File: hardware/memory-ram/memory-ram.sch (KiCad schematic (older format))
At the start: 27 parts, among them J1 Conn_Mem_Ext, J2 Conn_Power, U1 IS61WV5128EDBLL-10TLI, U2 74LVC1G86, U3 MIC5504-3.3YM5, U4 74LVC1G32, U5 74LVC1G332, U6 74LVC1G86, U7 74LVC1G04

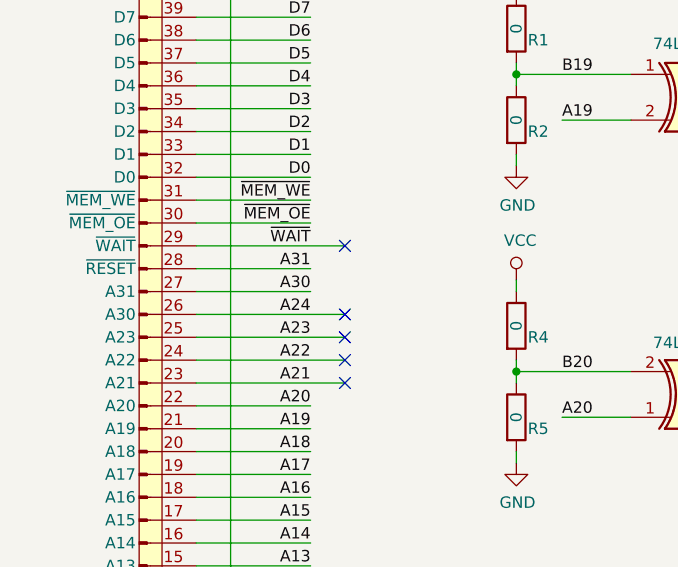
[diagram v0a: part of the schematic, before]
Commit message: Added ~RESET to memory bus
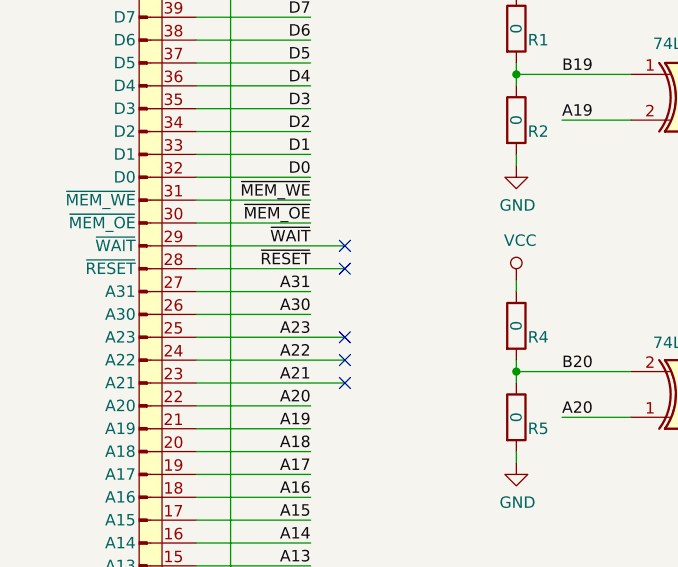
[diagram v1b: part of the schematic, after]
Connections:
- net A24 is gone; now on net A30: J1.26 (A30)
- net A30: no longer J1.27 (A31)
- net A31: now also J1.27 (A31); no longer J1.28 (~RESET)
- new net ~RESET: J1.28 (~RESET)
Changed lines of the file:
@@
 Text Label 1750 3600 2    50   ~ 0
 A23
-Text Label 1750 3500 2    50   ~ 0
-A24
 Text Label 1750 3200 2    50   ~ 0
 ~WAIT
@@
 Wire Wire Line
 	1750 4200 1250 4200
-Text Label 1750 3300 2    50   ~ 0
+Text Label 1750 3400 2    50   ~ 0
 A31
-Text Label 1750 3400 2    50   ~ 0
+Text Label 1750 3500 2    50   ~ 0
 A30
 Wire Wire Line
-	1750 3300 1250 3300
-Wire Wire Line
-	1250 3400 1750 3400
+	1750 3400 1250 3400
+Wire Wire Line
+	1250 3500 1750 3500
 $Comp
 L riscv-serial:Conn_Power J?
@@
 Wire Wire Line
 	1250 3600 1900 3600
-Wire Wire Line
-	1250 3500 1900 3500
-NoConn ~ 1900 3500
 NoConn ~ 1900 3600
 NoConn ~ 1900 3700
@@
 	5600 6550 4850 6550
 Connection ~ 4850 6550
+Wire Wire Line
+	1250 3300 1900 3300
+NoConn ~ 1900 3300
+Text Label 1750 3300 2    50   ~ 0
+~RESET
 $EndSCHEMATC

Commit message: Unified footprints
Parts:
- D1: footprint LED_SMD:LED_0805_2012Metric -> LED_SMD:LED_0805_2012Metric_Pad1.15x1.40mm_HandSolder
- R1, R2, R3, R4, R5: footprint Resistor_SMD:R_0805_2012Metric -> Resistor_SMD:R_0805_2012Metric_Pad1.15x1.40mm_HandSolder
- U2, U3, U4, U6, U7: footprint Package_TO_SOT_SMD:SOT-23-5 -> Package_TO_SOT_SMD:SOT-23-5_HandSoldering
- U5: footprint Package_TO_SOT_SMD:SOT-23-6 -> Package_TO_SOT_SMD:SOT-23-6_Handsoldering
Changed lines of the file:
@@
 F 0 "U3" H 7900 6117 50  0000 C CNN
 F 1 "MIC5504-3.3YM5" H 7900 6026 50  0000 C CNN
-F 2 "Package_TO_SOT_SMD:SOT-23-5" H 7900 5350 50  0001 C CNN
+F 2 "Package_TO_SOT_SMD:SOT-23-5_HandSoldering" H 7900 5350 50  0001 C CNN
 F 3 "http://ww1.microchip.com/downloads/en/DeviceDoc/MIC550X.pdf" H 7650 6000 50  0001 C CNN
 	1    7900 5750
@@
 F 0 "U5" H 5500 3033 50  0000 C CNN
 F 1 "74LVC1G332" H 5500 3124 50  0000 C CNN
-F 2 "Package_TO_SOT_SMD:SOT-23-6" H 5470 3320 50  0001 C CNN
+F 2 "Package_TO_SOT_SMD:SOT-23-6_Handsoldering" H 5470 3320 50  0001 C CNN
 F 3 "" H 5470 3320 50  0001 C CNN
 	1    5500 3350
@@
 F 0 "R1" H 2700 2200 50  0000 L CNN
 F 1 "0" V 2650 2250 50  0000 C CNN
-F 2 "Resistor_SMD:R_0805_2012Metric" V 2580 2250 50  0001 C CNN
+F 2 "Resistor_SMD:R_0805_2012Metric_Pad1.15x1.40mm_HandSolder" V 2580 2250 50  0001 C CNN
 F 3 "~" H 2650 2250 50  0001 C CNN
 	1    2650 2250
@@
 F 0 "R2" H 2700 2600 50  0000 L CNN
 F 1 "0" V 2650 2650 50  0000 C CNN
-F 2 "Resistor_SMD:R_0805_2012Metric" V 2580 2650 50  0001 C CNN
+F 2 "Resistor_SMD:R_0805_2012Metric_Pad1.15x1.40mm_HandSolder" V 2580 2650 50  0001 C CNN
 F 3 "~" H 2650 2650 50  0001 C CNN
 	1    2650 2650
@@
 F 0 "R4" H 2700 3500 50  0000 L CNN
 F 1 "0" V 2650 3550 50  0000 C CNN
-F 2 "Resistor_SMD:R_0805_2012Metric" V 2580 3550 50  0001 C CNN
+F 2 "Resistor_SMD:R_0805_2012Metric_Pad1.15x1.40mm_HandSolder" V 2580 3550 50  0001 C CNN
 F 3 "~" H 2650 3550 50  0001 C CNN
 	1    2650 3550
@@
 F 0 "R5" H 2700 3900 50  0000 L CNN
 F 1 "0" V 2650 3950 50  0000 C CNN
-F 2 "Resistor_SMD:R_0805_2012Metric" V 2580 3950 50  0001 C CNN
+F 2 "Resistor_SMD:R_0805_2012Metric_Pad1.15x1.40mm_HandSolder" V 2580 3950 50  0001 C CNN
 F 3 "~" H 2650 3950 50  0001 C CNN
 	1    2650 3950
@@
 F 0 "U4" H 4400 3600 50  0000 C CNN
 F 1 "74LVC1G32" H 4400 3484 50  0000 C CNN
-F 2 "Package_TO_SOT_SMD:SOT-23-5" H 4370 3220 50  0001 C CNN
+F 2 "Package_TO_SOT_SMD:SOT-23-5_HandSoldering" H 4370 3220 50  0001 C CNN
 F 3 "" H 4370 3220 50  0001 C CNN
 	1    4400 3250
@@
 F 0 "U6" H 3450 3533 50  0000 C CNN
 F 1 "74LVC1G86" H 3450 3624 50  0000 C CNN
-F 2 "Package_TO_SOT_SMD:SOT-23-5" H 3420 3820 50  0001 C CNN
+F 2 "Package_TO_SOT_SMD:SOT-23-5_HandSoldering" H 3420 3820 50  0001 C CNN
 F 3 "" H 3420 3820 50  0001 C CNN
 	1    3450 3850
@@
 F 0 "U2" H 3450 2875 50  0000 C CNN
 F 1 "74LVC1G86" H 3450 2784 50  0000 C CNN
-F 2 "Package_TO_SOT_SMD:SOT-23-5" H 3420 2520 50  0001 C CNN
+F 2 "Package_TO_SOT_SMD:SOT-23-5_HandSoldering" H 3420 2520 50  0001 C CNN
 F 3 "" H 3420 2520 50  0001 C CNN
 	1    3450 2550
@@
 F 0 "U2" H 3530 5996 50  0000 L CNN
 F 1 "74LVC1G86" H 3530 5905 50  0000 L CNN
-F 2 "Package_TO_SOT_SMD:SOT-23-5" H 3370 5920 50  0001 C CNN
+F 2 "Package_TO_SOT_SMD:SOT-23-5_HandSoldering" H 3370 5920 50  0001 C CNN
 F 3 "" H 3370 5920 50  0001 C CNN
 	2    3400 5950
@@
 F 0 "U6" H 4280 5996 50  0000 L CNN
 F 1 "74LVC1G86" H 4280 5905 50  0000 L CNN
-F 2 "Package_TO_SOT_SMD:SOT-23-5" H 4120 5920 50  0001 C CNN
+F 2 "Package_TO_SOT_SMD:SOT-23-5_HandSoldering" H 4120 5920 50  0001 C CNN
 F 3 "" H 4120 5920 50  0001 C CNN
 	2    4150 5950
@@
 F 0 "U4" H 5050 6050 50  0000 C CNN
 F 1 "74LVC1G32" H 5200 5950 50  0000 C CNN
-F 2 "Package_TO_SOT_SMD:SOT-23-5" H 4820 5920 50  0001 C CNN
+F 2 "Package_TO_SOT_SMD:SOT-23-5_HandSoldering" H 4820 5920 50  0001 C CNN
 F 3 "" H 4820 5920 50  0001 C CNN
 	2    4850 5950
@@
 F 0 "U5" H 2780 5996 50  0000 L CNN
 F 1 "74LVC1G332" H 2780 5905 50  0000 L CNN
-F 2 "Package_TO_SOT_SMD:SOT-23-6" H 2620 5920 50  0001 C CNN
+F 2 "Package_TO_SOT_SMD:SOT-23-6_Handsoldering" H 2620 5920 50  0001 C CNN
 F 3 "" H 2620 5920 50  0001 C CNN
 	2    2650 5950
@@
 F 0 "R3" H 10150 2950 50  0000 L CNN
 F 1 "330" V 10100 3000 50  0000 C CNN
-F 2 "Resistor_SMD:R_0805_2012Metric" V 10030 3000 50  0001 C CNN
+F 2 "Resistor_SMD:R_0805_2012Metric_Pad1.15x1.40mm_HandSolder" V 10030 3000 50  0001 C CNN
 F 3 "~" H 10100 3000 50  0001 C CNN
 	1    10100 3000
@@
 F 0 "D1" V 10138 2383 50  0000 R CNN
 F 1 "LED" V 10047 2383 50  0000 R CNN
-F 2 "LED_SMD:LED_0805_2012Metric" H 10100 2500 50  0001 C CNN
+F 2 "LED_SMD:LED_0805_2012Metric_Pad1.15x1.40mm_HandSolder" H 10100 2500 50  0001 C CNN
 F 3 "~" H 10100 2500 50  0001 C CNN
 	1    10100 2500
@@
 F 0 "U7" H 4400 3550 50  0000 C CNN
 F 1 "74LVC1G04" H 4400 3650 50  0000 C CNN
-F 2 "Package_TO_SOT_SMD:SOT-23-5" H 4400 3850 50  0001 C CNN
+F 2 "Package_TO_SOT_SMD:SOT-23-5_HandSoldering" H 4400 3850 50  0001 C CNN
 F 3 "" H 4400 3850 50  0001 C CNN
 	1    4400 3850
@@
 F 0 "U7" H 5800 6000 50  0000 C CNN
 F 1 "74LVC1G04" H 5950 5900 50  0000 C CNN
-F 2 "Package_TO_SOT_SMD:SOT-23-5" H 5600 5950 50  0001 C CNN
+F 2 "Package_TO_SOT_SMD:SOT-23-5_HandSoldering" H 5600 5950 50  0001 C CNN
 F 3 "" H 5600 5950 50  0001 C CNN
 	2    5600 5950

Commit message: Added test points
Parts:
- added TP1: TestPoint, TestPoint:TestPoint_THTPad_D2.0mm_Drill1.0mm, symbol Connector:TestPoint
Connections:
- net GND: now also TP1.1
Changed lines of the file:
@@
 	8150 1800 8400 1800
 $Comp
-L power:VCC #PWR01
+L power:VCC #PWR?
 U 1 1 5ED06DC6
 P 7550 1550
-F 0 "#PWR01" H 7550 1400 50  0001 C CNN
+F 0 "#PWR?" H 7550 1400 50  0001 C CNN
 F 1 "VCC" H 7567 1723 50  0000 C CNN
 F 2 "" H 7550 1550 50  0001 C CNN
@@
 	7550 1550 7550 1600
 $Comp
-L power:GND #PWR03
+L power:GND #PWR?
 U 1 1 5ED072CF
 P 7550 4250
-F 0 "#PWR03" H 7550 4000 50  0001 C CNN
+F 0 "#PWR?" H 7550 4000 50  0001 C CNN
 F 1 "GND" H 7555 4077 50  0000 C CNN
 F 2 "" H 7550 4250 50  0001 C CNN
@@
 P 1400 6100
 AR Path="/5ED0998A/5ED5DB0E" Ref="#PWR?"  Part="1"
-AR Path="/5ED5DB0E" Ref="#PWR05"  Part="1"
-F 0 "#PWR05" H 1400 5850 50  0001 C CNN
+AR Path="/5ED5DB0E" Ref="#PWR?"  Part="1"
+F 0 "#PWR?" H 1400 5850 50  0001 C CNN
 F 1 "GND" H 1405 5927 50  0000 C CNN
 F 2 "" H 1400 6100 50  0001 C CNN
@@
 P 8450 5600
 AR Path="/5ED0998A/5ED661B1" Ref="#PWR?"  Part="1"
-AR Path="/5ED661B1" Ref="#PWR06"  Part="1"
-F 0 "#PWR06" H 8450 5450 50  0001 C CNN
+AR Path="/5ED661B1" Ref="#PWR?"  Part="1"
+F 0 "#PWR?" H 8450 5450 50  0001 C CNN
 F 1 "VCC" H 8467 5773 50  0000 C CNN
 F 2 "" H 8450 5600 50  0001 C CNN
@@
 P 6700 6250
 AR Path="/5ED0998A/5ED661B9" Ref="#PWR?"  Part="1"
-AR Path="/5ED661B9" Ref="#PWR07"  Part="1"
-F 0 "#PWR07" H 6700 6000 50  0001 C CNN
+AR Path="/5ED661B9" Ref="#PWR?"  Part="1"
+F 0 "#PWR?" H 6700 6000 50  0001 C CNN
 F 1 "GND" H 6705 6077 50  0000 C CNN
 F 2 "" H 6700 6250 50  0001 C CNN
@@
 P 7900 6250
 AR Path="/5ED0998A/5ED661D1" Ref="#PWR?"  Part="1"
-AR Path="/5ED661D1" Ref="#PWR08"  Part="1"
-F 0 "#PWR08" H 7900 6000 50  0001 C CNN
+AR Path="/5ED661D1" Ref="#PWR?"  Part="1"
+F 0 "#PWR?" H 7900 6000 50  0001 C CNN
 F 1 "GND" H 7905 6077 50  0000 C CNN
 F 2 "" H 7900 6250 50  0001 C CNN
@@
 P 2650 6600
 AR Path="/5ED0998A/5EED200D" Ref="#PWR?"  Part="1"
-AR Path="/5EED200D" Ref="#PWR010"  Part="1"
-F 0 "#PWR010" H 2650 6350 50  0001 C CNN
+AR Path="/5EED200D" Ref="#PWR?"  Part="1"
+F 0 "#PWR?" H 2650 6350 50  0001 C CNN
 F 1 "GND" H 2655 6427 50  0000 C CNN
 F 2 "" H 2650 6600 50  0001 C CNN
@@
 P 2650 5300
 AR Path="/5ED0998A/5EEDBEC3" Ref="#PWR?"  Part="1"
-AR Path="/5EEDBEC3" Ref="#PWR09"  Part="1"
-F 0 "#PWR09" H 2650 5150 50  0001 C CNN
+AR Path="/5EEDBEC3" Ref="#PWR?"  Part="1"
+F 0 "#PWR?" H 2650 5150 50  0001 C CNN
 F 1 "VCC" H 2667 5473 50  0000 C CNN
 F 2 "" H 2650 5300 50  0001 C CNN
@@
 	1400 6000 1400 6100
 $Comp
-L power:PWR_FLAG #FLG0101
+L power:PWR_FLAG #FLG?
 U 1 1 5ECA3460
 P 7100 6250
-F 0 "#FLG0101" H 7100 6325 50  0001 C CNN
+F 0 "#FLG?" H 7100 6325 50  0001 C CNN
 F 1 "PWR_FLAG" H 7100 6423 50  0000 C CNN
 F 2 "" H 7100 6250 50  0001 C CNN
@@
 	7100 5550 7100 5650
 $Comp
-L power:PWR_FLAG #FLG0102
+L power:PWR_FLAG #FLG?
 U 1 1 5ECB86FC
 P 7100 5550
-F 0 "#FLG0102" H 7100 5625 50  0001 C CNN
+F 0 "#FLG?" H 7100 5625 50  0001 C CNN
 F 1 "PWR_FLAG" H 7100 5724 50  0000 C CNN
 F 2 "" H 7100 5550 50  0001 C CNN
@@
 Connection ~ 2650 2450
 $Comp
-L power:GND #PWR011
+L power:GND #PWR?
 U 1 1 5EDCC7A6
 P 2650 2850
-F 0 "#PWR011" H 2650 2600 50  0001 C CNN
+F 0 "#PWR?" H 2650 2600 50  0001 C CNN
 F 1 "GND" H 2655 2677 50  0000 C CNN
 F 2 "" H 2650 2850 50  0001 C CNN
@@
 	2650 2800 2650 2850
 $Comp
-L power:VCC #PWR02
+L power:VCC #PWR?
 U 1 1 5EDD6C18
 P 2650 2050
-F 0 "#PWR02" H 2650 1900 50  0001 C CNN
+F 0 "#PWR?" H 2650 1900 50  0001 C CNN
 F 1 "VCC" H 2667 2223 50  0000 C CNN
 F 2 "" H 2650 2050 50  0001 C CNN
@@
 Connection ~ 2650 3750
 $Comp
-L power:GND #PWR013
+L power:GND #PWR?
 U 1 1 5EE1F78E
 P 2650 4150
-F 0 "#PWR013" H 2650 3900 50  0001 C CNN
+F 0 "#PWR?" H 2650 3900 50  0001 C CNN
 F 1 "GND" H 2655 3977 50  0000 C CNN
 F 2 "" H 2650 4150 50  0001 C CNN
@@
 	2650 4100 2650 4150
 $Comp
-L power:VCC #PWR012
+L power:VCC #PWR?
 U 1 1 5EE1F795
 P 2650 3350
-F 0 "#PWR012" H 2650 3200 50  0001 C CNN
+F 0 "#PWR?" H 2650 3200 50  0001 C CNN
 F 1 "VCC" H 2667 3523 50  0000 C CNN
 F 2 "" H 2650 3350 50  0001 C CNN
@@
 	10100 2650 10100 2850
 $Comp
-L power:VCC #PWR04
+L power:VCC #PWR?
 U 1 1 5EF298E7
 P 10100 2250
-F 0 "#PWR04" H 10100 2100 50  0001 C CNN
+F 0 "#PWR?" H 10100 2100 50  0001 C CNN
 F 1 "VCC" H 10117 2423 50  0000 C CNN
 F 2 "" H 10100 2250 50  0001 C CNN
@@
 Text Label 1750 3300 2    50   ~ 0
 ~RESET
+$Comp
+L Connector:TestPoint TP1
+U 1 1 5F053D0E
+P 9100 2250
+F 0 "TP1" H 9158 2370 50  0000 L CNN
+F 1 "TestPoint" H 9158 2279 50  0000 L CNN
+F 2 "TestPoint:TestPoint_THTPad_D2.0mm_Drill1.0mm" H 9300 2250 50  0001 C CNN
+F 3 "~" H 9300 2250 50  0001 C CNN
+	1    9100 2250
+	1    0    0    -1
+$EndComp
+$Comp
+L power:GND #PWR?
+U 1 1 5F053DC6
+P 9100 2350
+F 0 "#PWR?" H 9100 2100 50  0001 C CNN
+F 1 "GND" H 9105 2177 50  0000 C CNN
+F 2 "" H 9100 2350 50  0001 C CNN
+F 3 "" H 9100 2350 50  0001 C CNN
+	1    9100 2350
+	1    0    0    -1
+$EndComp
+Wire Wire Line
+	9100 2250 9100 2350
 $EndSCHEMATC
